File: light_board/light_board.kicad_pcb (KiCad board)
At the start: 2 copper layers, 36 x 34 mm, 17 parts, among them J1 CONN_01X02, J2 Screw_Terminal_1x02, J3 Screw_Terminal_1x02, Q1 FDC658AP, U1 LM3409MY

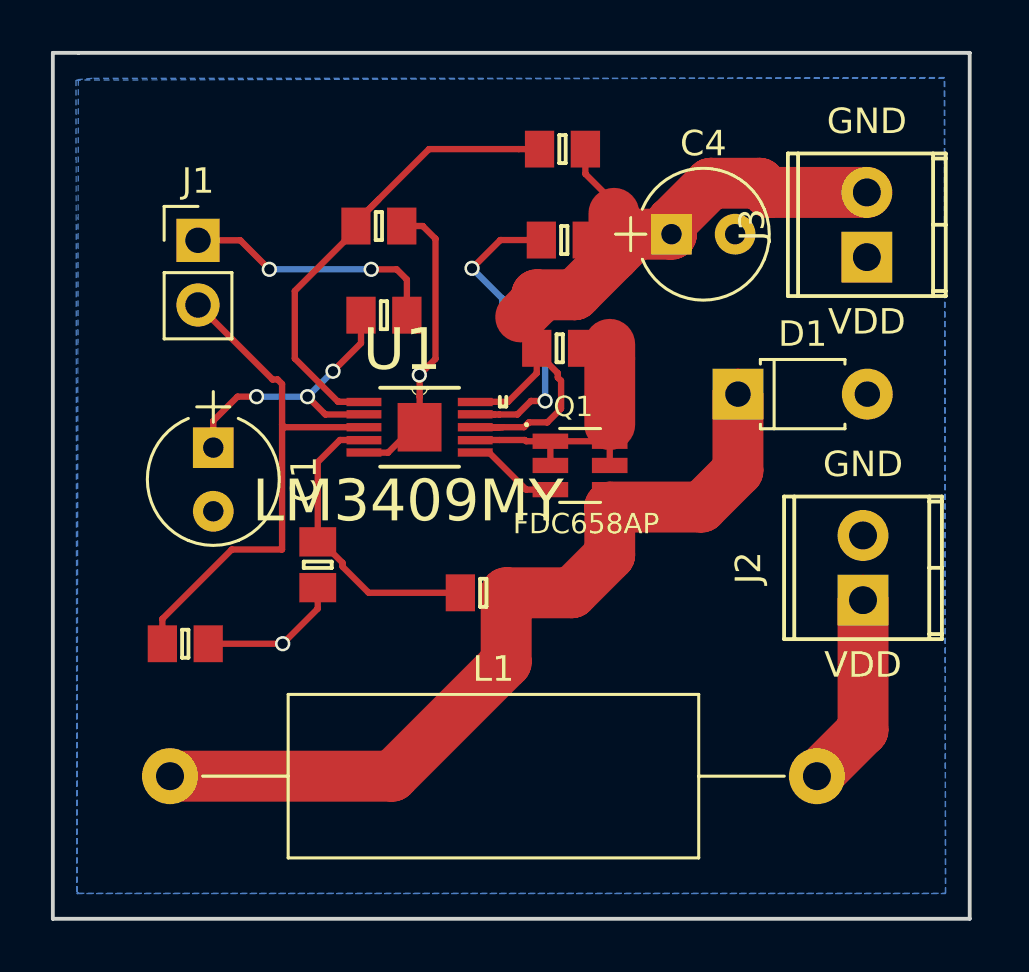
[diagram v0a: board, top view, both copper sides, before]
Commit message: changed design to use large resistor
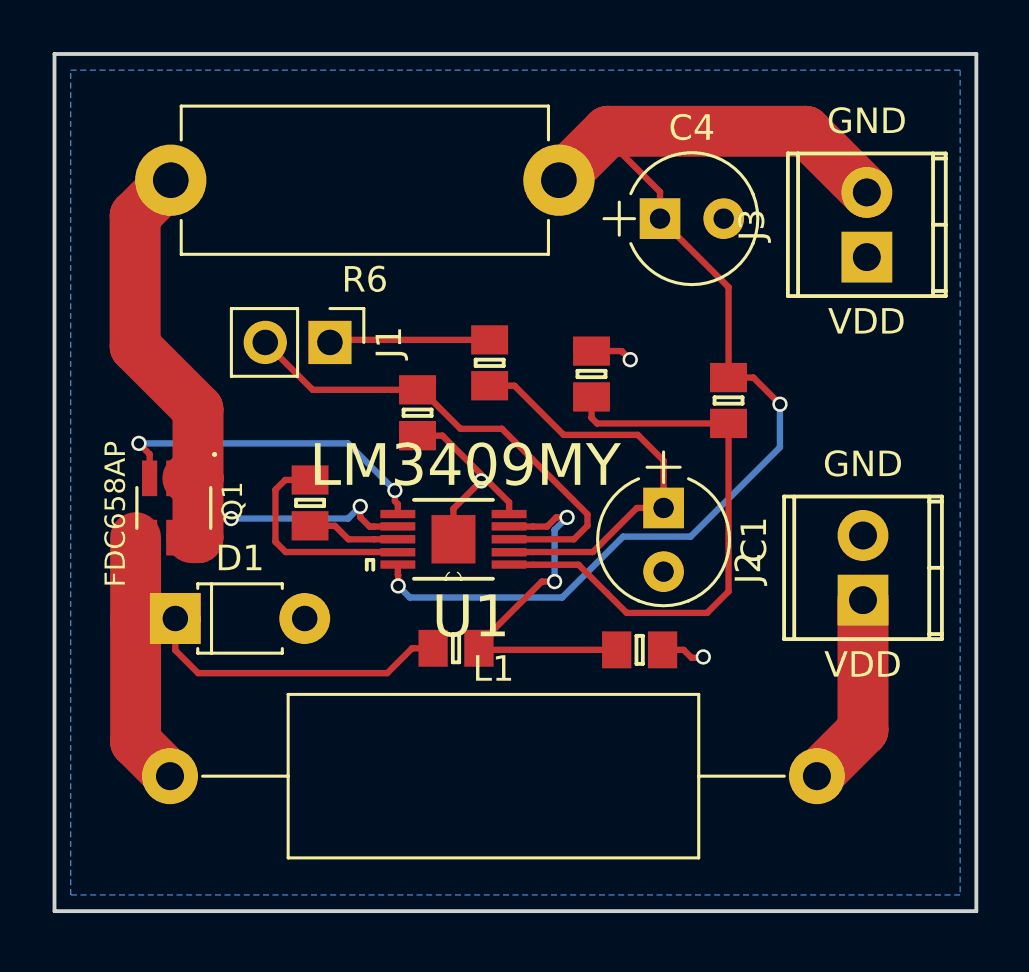
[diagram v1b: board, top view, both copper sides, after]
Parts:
- R6: value 0.12R -> 0.1R; footprint agg:0805 -> Resistors_THT:R_Axial_DIN0614_L14.3mm_D5.7mm_P15.24mm_Horizontal
- moved D1 23.8 mm to (143.8, 128.2)
- moved C1 17.8 mm to (163.0, 123.9)
- moved Q1 16.0 mm to (143.8, 123.9), turned to 270 degrees
- moved C2 14.4 mm to (149.1, 123.7), turned to 270 degrees
- moved C3 13.1 mm to (162.0, 129.4), turned to 0 degrees
- moved R2 12.9 mm to (153.3, 120.1), turned to 270 degrees
- moved R5 11.8 mm to (165.5, 119.7), turned to 90 degrees
- moved R4 10.2 mm to (160.2, 118.6), turned to 90 degrees
- moved R6 6.60 mm to (158.9, 111.0), turned to 180 degrees
- moved J1 6.55 mm to (149.9, 117.4), turned to 270 degrees
- moved U1 4.60 mm to (154.7, 125.1), turned to 180 degrees
- moved R1 4.55 mm to (156.2, 118.2), turned to 90 degrees
- moved R3 2.43 mm to (154.8, 129.4), turned to 0 degrees
- moved C4 0.76 mm to (162.8, 112.5)
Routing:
- net /CSP: track 36.4 -> 51.8 mm, vias 0 -> 2
- net /CSN: track 12.8 -> 25.2 mm, vias 0 -> 2
- net Net-(D1-Pad1): track 35.5 -> 23.7 mm
- net /PGATE: track 3.55 -> 13.3 mm, vias 0 -> 2
- net GND: track 17.6 -> 11.8 mm, vias 2 -> 3
- net Net-(C2-Pad1): track 14.0 -> 8.54 mm, vias 2 -> 0
- net Net-(C1-Pad1): track 11.7 -> 16.7 mm, vias 3 -> 0
- net Net-(J1-Pad1): track 10.2 -> 6.31 mm, vias 2 -> 0
- net /UVLO: track 19.4 -> 22.6 mm
- net /COFF: track 11.8 -> 14.7 mm, vias 0 -> 2
- net Net-(J1-Pad2): track 21.1 -> 19.2 mm
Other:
- board size 36 x 34 mm -> 36.2 x 33.7 mm
